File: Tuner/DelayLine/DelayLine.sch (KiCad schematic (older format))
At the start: 87 parts, among them J1 Conn_Coaxial, J10 Conn_Coaxial, J11 Conn_Coaxial, J12 Conn_Coaxial, J13 Conn_01x01, J14 Conn_01x01, J15 Conn_01x01, J16 Conn_01x01, J17 Conn_02x10_Odd_Even, J18 Conn_Coaxial, J19 Conn_Coaxial, J2 Conn_01x01, J20 Conn_Coaxial, J21 Conn_Coaxial, J22 Conn_Coaxial, J23 Conn_Coaxial, J24 Conn_01x01, J25 Conn_01x01, J26 Conn_01x01, J27 Conn_01x01, J28 Conn_01x01, J29 Conn_Coaxial, J3 Conn_Coaxial, J31 Conn_Coaxial, J32 Conn_01x01, J33 Conn_01x01, J34 Conn_01x01, J35 Conn_01x01, J5 Conn_Coaxial, J6 Conn_Coaxial, J7 Conn_Coaxial, J8 Conn_01x02, J9 Conn_01x02

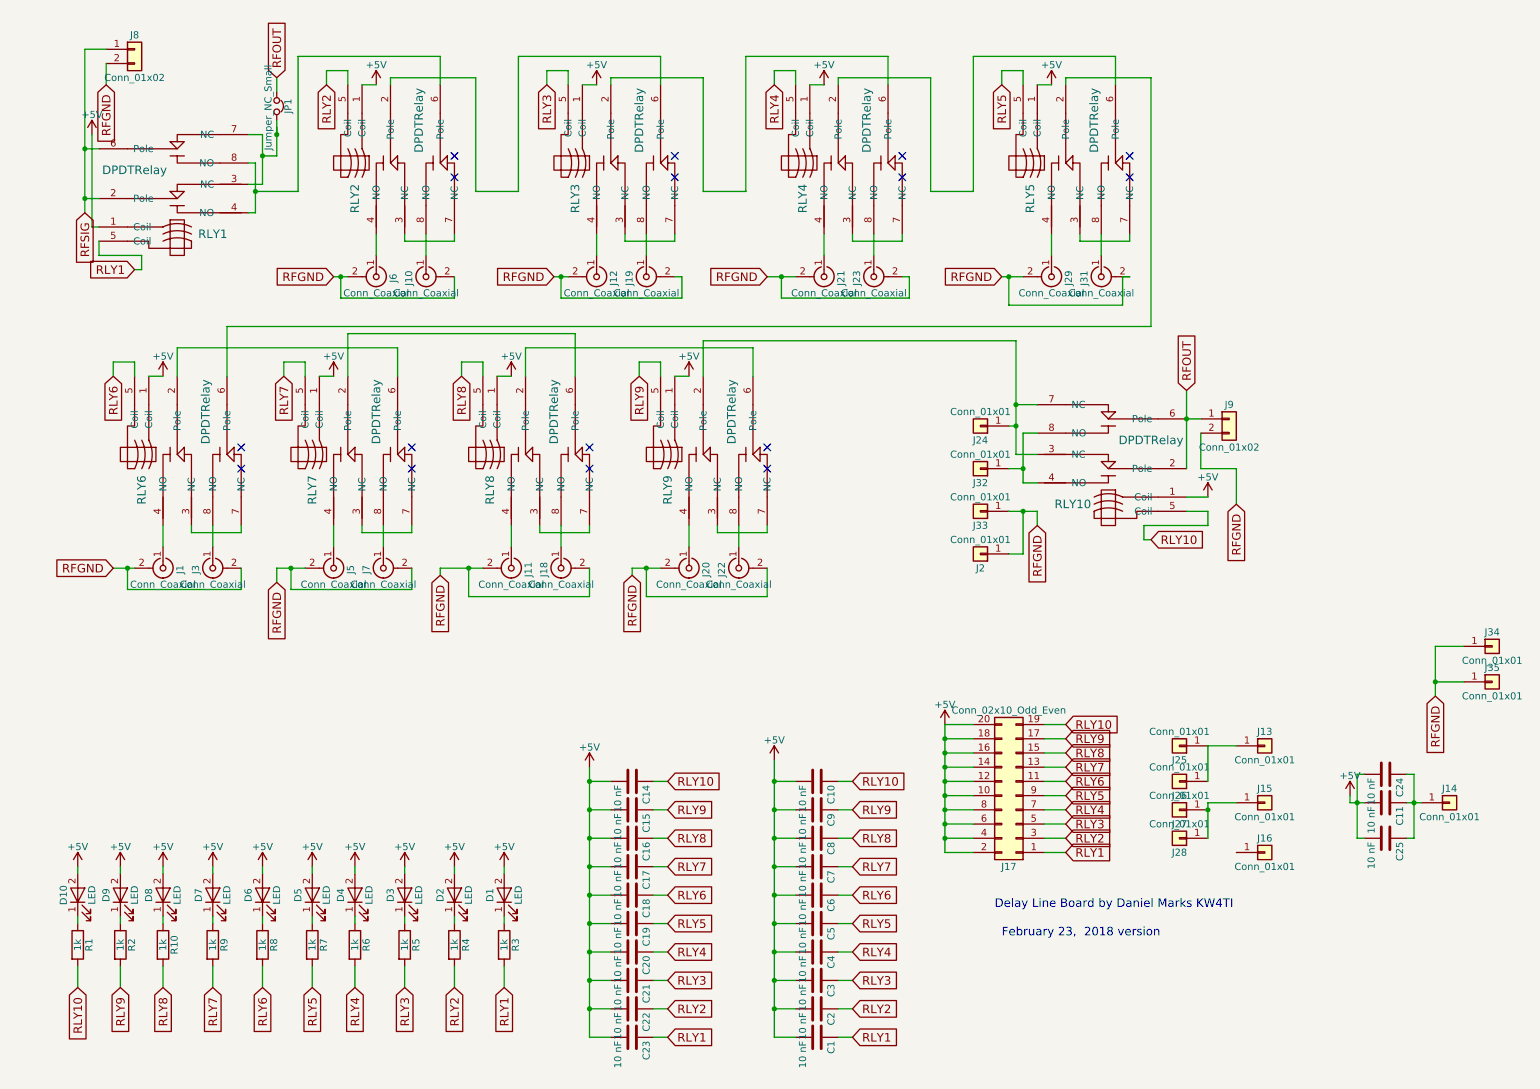
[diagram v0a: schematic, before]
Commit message: Changed bypass method on delay lines
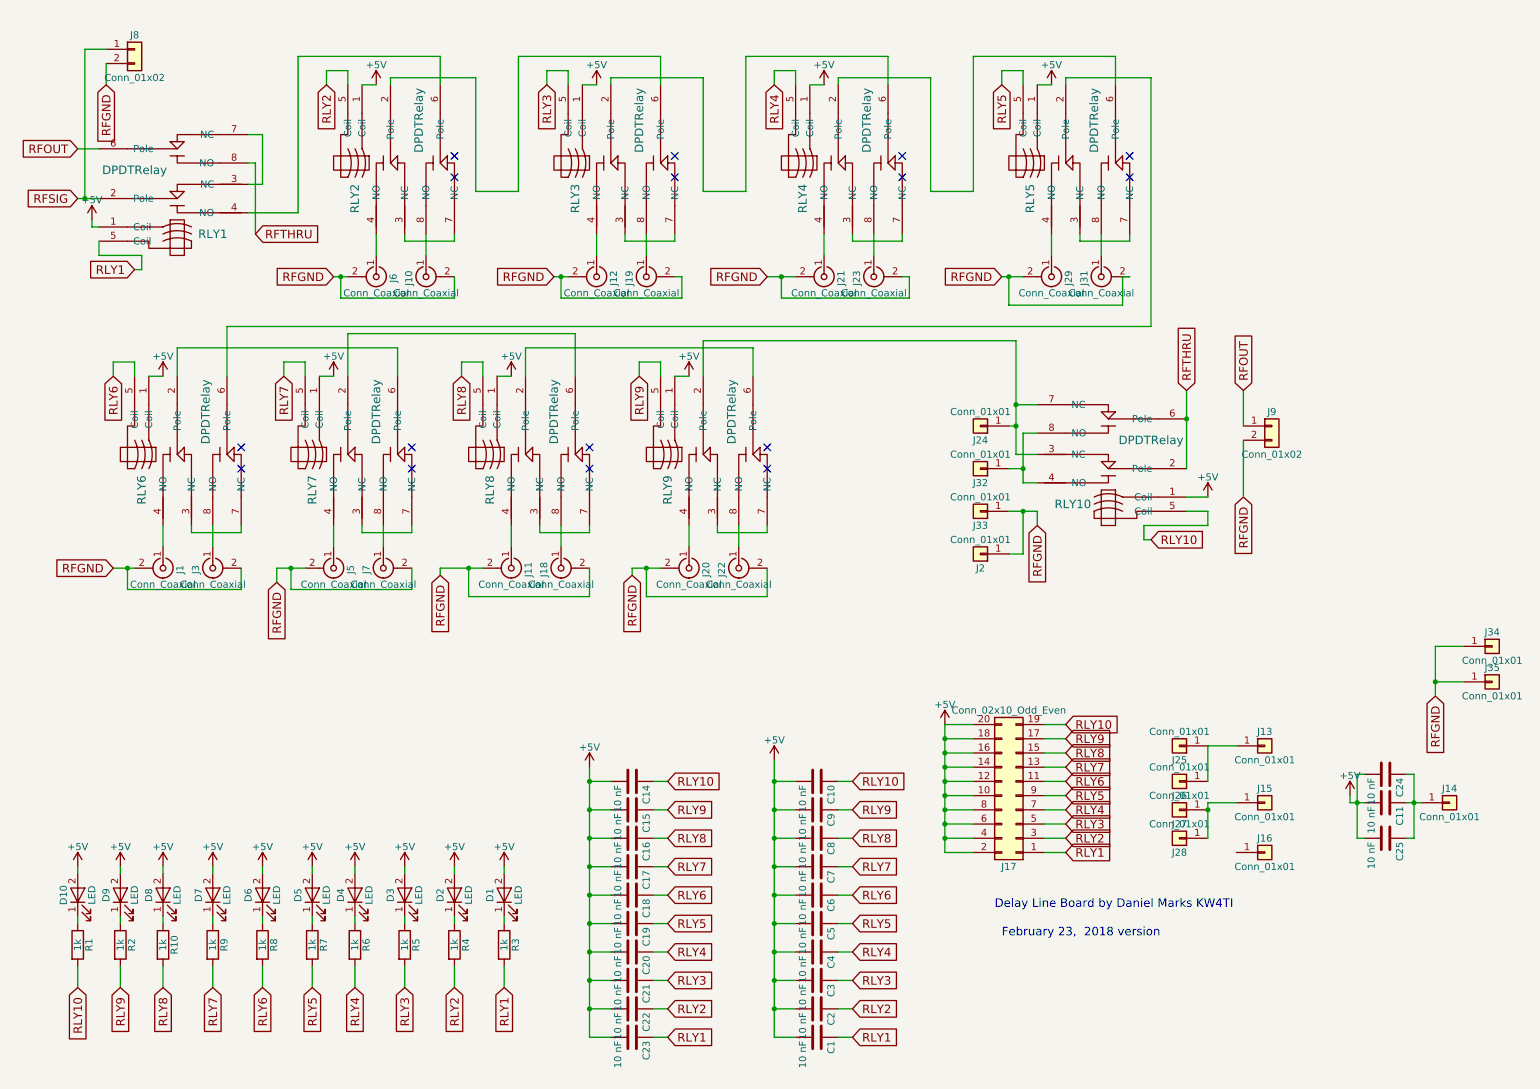
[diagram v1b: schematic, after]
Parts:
- removed JP1: Jumper_NC_Small, Pin_Headers:Pin_Header_Straight_1x02_Pitch2.54mm, symbol Jumper_NC_Small
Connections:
- net RFOUT: now also RLY1.6 (Pole); no longer RLY10.2 (Pole), RLY10.6 (Pole)
- net RFSIG: no longer RLY1.6 (Pole)
- net at RLY1.4 (NO), RLY2.6 (Pole): no longer RLY1.8 (NO)
- new net RFTHRU: RLY1.8 (NO), RLY10.2 (Pole), RLY10.6 (Pole)
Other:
- moved on the sheet: J9

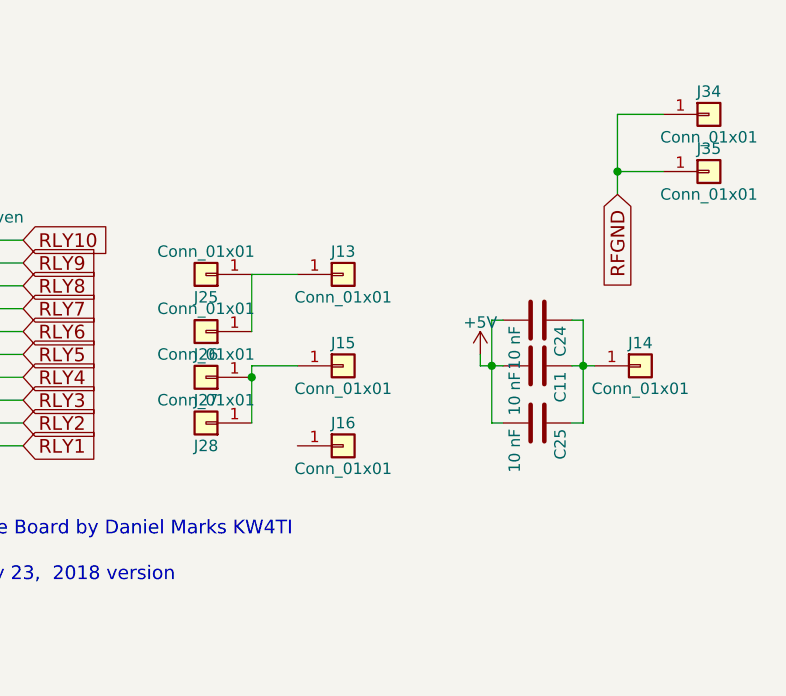
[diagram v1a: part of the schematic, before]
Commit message: Added extra capacitors between relay power and ground posts
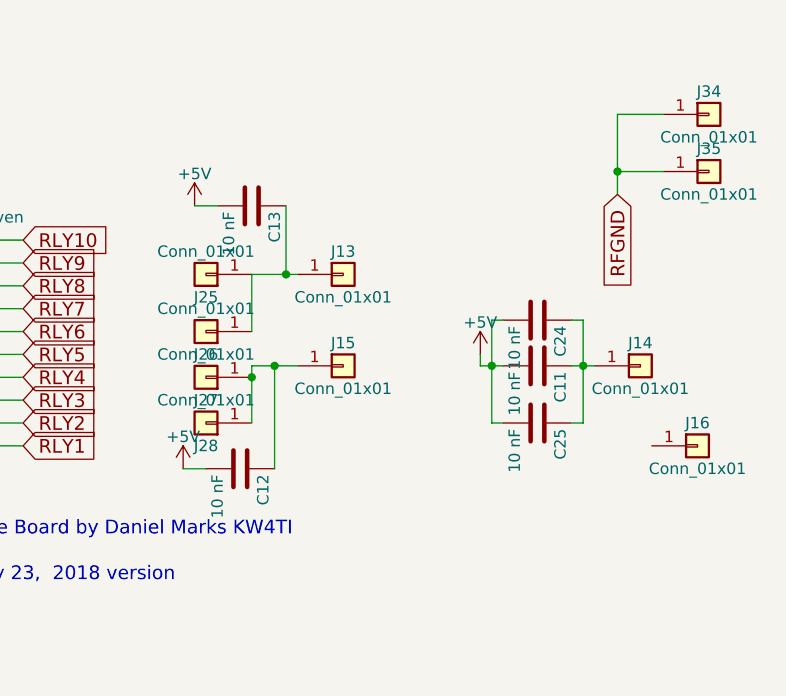
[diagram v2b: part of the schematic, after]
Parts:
- added C12, C13: 10 nF, Capacitors_THT:C_Disc_D5.0mm_W2.5mm_P2.50mm, symbol C
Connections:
- net +5V: now also C12.2, C13.2
- net at J13.1 (Pin_1), J25.1 (Pin_1), J26.1 (Pin_1): now also C13.1
- net at J15.1 (Pin_1), J27.1 (Pin_1), J28.1 (Pin_1): now also C12.1
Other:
- moved on the sheet: J16
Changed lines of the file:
@@
 $EndComp
 $Comp
-L +5V #PWR01
+L +5V #PWR2
 U 1 1 5B1A4DAD
 P 950 1850
-F 0 "#PWR01" H 950 1700 50  0001 C CNN
+F 0 "#PWR2" H 950 1700 50  0001 C CNN
 F 1 "+5V" H 950 1990 50  0000 C CNN
 F 2 "" H 950 1850 50  0001 C CNN
@@
 $EndComp
 $Comp
-L +5V #PWR02
+L +5V #PWR5
 U 1 1 5B25DE9C
 P 1450 6400
-F 0 "#PWR02" H 1450 6250 50  0001 C CNN
+F 0 "#PWR5" H 1450 6250 50  0001 C CNN
 F 1 "+5V" H 1450 6540 50  0000 C CNN
 F 2 "" H 1450 6400 50  0001 C CNN
@@
 $EndComp
 $Comp
-L +5V #PWR03
+L +5V #PWR6
 U 1 1 5B25F712
 P 1800 6400
-F 0 "#PWR03" H 1800 6250 50  0001 C CNN
+F 0 "#PWR6" H 1800 6250 50  0001 C CNN
 F 1 "+5V" H 1800 6540 50  0000 C CNN
 F 2 "" H 1800 6400 50  0001 C CNN
@@
 $EndComp
 $Comp
-L +5V #PWR04
+L +5V #PWR7
 U 1 1 5B25F91B
 P 2150 6400
-F 0 "#PWR04" H 2150 6250 50  0001 C CNN
+F 0 "#PWR7" H 2150 6250 50  0001 C CNN
 F 1 "+5V" H 2150 6540 50  0000 C CNN
 F 2 "" H 2150 6400 50  0001 C CNN
@@
 $EndComp
 $Comp
-L +5V #PWR05
+L +5V #PWR8
 U 1 1 5B25F931
 P 2500 6400
-F 0 "#PWR05" H 2500 6250 50  0001 C CNN
+F 0 "#PWR8" H 2500 6250 50  0001 C CNN
 F 1 "+5V" H 2500 6540 50  0000 C CNN
 F 2 "" H 2500 6400 50  0001 C CNN
@@
 $EndComp
 $Comp
-L +5V #PWR06
+L +5V #PWR10
 U 1 1 5B25FB4D
 P 2800 6400
-F 0 "#PWR06" H 2800 6250 50  0001 C CNN
+F 0 "#PWR10" H 2800 6250 50  0001 C CNN
 F 1 "+5V" H 2800 6540 50  0000 C CNN
 F 2 "" H 2800 6400 50  0001 C CNN
@@
 $EndComp
 $Comp
-L +5V #PWR07
+L +5V #PWR12
 U 1 1 5B25FB63
 P 3150 6400
-F 0 "#PWR07" H 3150 6250 50  0001 C CNN
+F 0 "#PWR12" H 3150 6250 50  0001 C CNN
 F 1 "+5V" H 3150 6540 50  0000 C CNN
 F 2 "" H 3150 6400 50  0001 C CNN
@@
 $EndComp
 $Comp
-L +5V #PWR08
+L +5V #PWR13
 U 1 1 5B25FB79
 P 3500 6400
-F 0 "#PWR08" H 3500 6250 50  0001 C CNN
+F 0 "#PWR13" H 3500 6250 50  0001 C CNN
 F 1 "+5V" H 3500 6540 50  0000 C CNN
 F 2 "" H 3500 6400 50  0001 C CNN
@@
 $EndComp
 $Comp
-L +5V #PWR09
+L +5V #PWR14
 U 1 1 5B25FB8F
 P 3850 6400
-F 0 "#PWR09" H 3850 6250 50  0001 C CNN
+F 0 "#PWR14" H 3850 6250 50  0001 C CNN
 F 1 "+5V" H 3850 6540 50  0000 C CNN
 F 2 "" H 3850 6400 50  0001 C CNN
@@
 RLY10
 $Comp
-L +5V #PWR010
+L +5V #PWR21
 U 1 1 5B89A678
 P 6950 5400
-F 0 "#PWR010" H 6950 5250 50  0001 C CNN
+F 0 "#PWR21" H 6950 5250 50  0001 C CNN
 F 1 "+5V" H 6950 5540 50  0000 C CNN
 F 2 "" H 6950 5400 50  0001 C CNN
@@
 $EndComp
 $Comp
-L +5V #PWR011
+L +5V #PWR3
 U 1 1 5B89BB19
 P 1150 6400
-F 0 "#PWR011" H 1150 6250 50  0001 C CNN
+F 0 "#PWR3" H 1150 6250 50  0001 C CNN
 F 1 "+5V" H 1150 6540 50  0000 C CNN
 F 2 "" H 1150 6400 50  0001 C CNN
@@
 $EndComp
 $Comp
-L +5V #PWR012
+L +5V #PWR1
 U 1 1 5B89BBCB
 P 850 6400
-F 0 "#PWR012" H 850 6250 50  0001 C CNN
+F 0 "#PWR1" H 850 6250 50  0001 C CNN
 F 1 "+5V" H 850 6540 50  0000 C CNN
 F 2 "" H 850 6400 50  0001 C CNN
@@
 RLY9
 $Comp
-L +5V #PWR013
+L +5V #PWR19
 U 1 1 5B89FB34
 P 5750 5650
-F 0 "#PWR013" H 5750 5500 50  0001 C CNN
+F 0 "#PWR19" H 5750 5500 50  0001 C CNN
 F 1 "+5V" H 5750 5790 50  0000 C CNN
 F 2 "" H 5750 5650 50  0001 C CNN
@@
 $EndComp
 $Comp
-L +5V #PWR014
+L +5V #PWR26
 U 1 1 5B97C780
 P 9800 5900
-F 0 "#PWR014" H 9800 5750 50  0001 C CNN
+F 0 "#PWR26" H 9800 5750 50  0001 C CNN
 F 1 "+5V" H 9800 6040 50  0000 C CNN
 F 2 "" H 9800 5900 50  0001 C CNN
@@
 RLY9
 $Comp
-L +5V #PWR015
+L +5V #PWR16
 U 1 1 5BA3849B
 P 4450 5700
-F 0 "#PWR015" H 4450 5550 50  0001 C CNN
+F 0 "#PWR16" H 4450 5550 50  0001 C CNN
 F 1 "+5V" H 4450 5840 50  0000 C CNN
 F 2 "" H 4450 5700 50  0001 C CNN
@@
 L Conn_01x01 J16
 U 1 1 5C727F83
-P 9200 6300
-F 0 "J16" H 9200 6400 50  0000 C CNN
-F 1 "Conn_01x01" H 9200 6200 50  0000 C CNN
-F 2 "Connectors:1pin" H 9200 6300 50  0001 C CNN
-F 3 "" H 9200 6300 50  0001 C CNN
-	1    9200 6300
+P 10750 6300
+F 0 "J16" H 10750 6400 50  0000 C CNN
+F 1 "Conn_01x01" H 10750 6200 50  0000 C CNN
+F 2 "Connectors:1pin" H 10750 6300 50  0001 C CNN
+F 3 "" H 10750 6300 50  0001 C CNN
+	1    10750 6300
 	1    0    0    -1
 $EndComp
@@
 RLY2
 $Comp
-L +5V #PWR016
+L +5V #PWR11
 U 1 1 5C733753
 P 2950 900
-F 0 "#PWR016" H 2950 750 50  0001 C CNN
+F 0 "#PWR11" H 2950 750 50  0001 C CNN
 F 1 "+5V" H 2950 1040 50  0000 C CNN
 F 2 "" H 2950 900 50  0001 C CNN
@@
 RLY10
 $Comp
-L +5V #PWR017
+L +5V #PWR25
 U 1 1 5C7350A4
 P 8800 3800
-F 0 "#PWR017" H 8800 3650 50  0001 C CNN
+F 0 "#PWR25" H 8800 3650 50  0001 C CNN
 F 1 "+5V" H 8800 3940 50  0000 C CNN
 F 2 "" H 8800 3800 50  0001 C CNN
@@
 RLY3
 $Comp
-L +5V #PWR018
+L +5V #PWR17
 U 1 1 5C759EA2
 P 4500 900
-F 0 "#PWR018" H 4500 750 50  0001 C CNN
+F 0 "#PWR17" H 4500 750 50  0001 C CNN
 F 1 "+5V" H 4500 1040 50  0000 C CNN
 F 2 "" H 4500 900 50  0001 C CNN
@@
 RLY4
 $Comp
-L +5V #PWR019
+L +5V #PWR20
 U 1 1 5C75A6EF
 P 6100 900
-F 0 "#PWR019" H 6100 750 50  0001 C CNN
+F 0 "#PWR20" H 6100 750 50  0001 C CNN
 F 1 "+5V" H 6100 1040 50  0000 C CNN
 F 2 "" H 6100 900 50  0001 C CNN
@@
 RLY5
 $Comp
-L +5V #PWR020
+L +5V #PWR22
 U 1 1 5C75AF8D
 P 7700 900
-F 0 "#PWR020" H 7700 750 50  0001 C CNN
+F 0 "#PWR22" H 7700 750 50  0001 C CNN
 F 1 "+5V" H 7700 1040 50  0000 C CNN
 F 2 "" H 7700 900 50  0001 C CNN
@@
 RLY6
 $Comp
-L +5V #PWR021
+L +5V #PWR4
 U 1 1 5C75CACE
 P 1450 2950
-F 0 "#PWR021" H 1450 2800 50  0001 C CNN
+F 0 "#PWR4" H 1450 2800 50  0001 C CNN
 F 1 "+5V" H 1450 3090 50  0000 C CNN
 F 2 "" H 1450 2950 50  0001 C CNN
@@
 RLY7
 $Comp
-L +5V #PWR022
+L +5V #PWR9
 U 1 1 5C75D7A5
 P 2650 2950
-F 0 "#PWR022" H 2650 2800 50  0001 C CNN
+F 0 "#PWR9" H 2650 2800 50  0001 C CNN
 F 1 "+5V" H 2650 3090 50  0000 C CNN
 F 2 "" H 2650 2950 50  0001 C CNN
@@
 RLY8
 $Comp
-L +5V #PWR023
+L +5V #PWR15
 U 1 1 5C75E937
 P 3900 2950
-F 0 "#PWR023" H 3900 2800 50  0001 C CNN
+F 0 "#PWR15" H 3900 2800 50  0001 C CNN
 F 1 "+5V" H 3900 3090 50  0000 C CNN
 F 2 "" H 3900 2950 50  0001 C CNN
@@
 RLY9
 $Comp
-L +5V #PWR024
+L +5V #PWR18
 U 1 1 5C75F12E
 P 5150 2950
-F 0 "#PWR024" H 5150 2800 50  0001 C CNN
+F 0 "#PWR18" H 5150 2800 50  0001 C CNN
 F 1 "+5V" H 5150 3090 50  0000 C CNN
 F 2 "" H 5150 2950 50  0001 C CNN
@@
 	900  650  1050 650
 Connection ~ 900  1700
+$Comp
+L +5V #PWR24
+U 1 1 5DDBBCDB
+P 8550 5250
+F 0 "#PWR24" H 8550 5100 50  0001 C CNN
+F 1 "+5V" H 8550 5390 50  0000 C CNN
+F 2 "" H 8550 5250 50  0001 C CNN
+F 3 "" H 8550 5250 50  0001 C CNN
+	1    8550 5250
+	1    0    0    -1
+$EndComp
+$Comp
+L C C13
+U 1 1 5DDBBF5C
+P 8800 5250
+F 0 "C13" H 8825 5350 50  0000 L CNN
+F 1 "10 nF" H 8825 5150 50  0000 L CNN
+F 2 "Capacitors_THT:C_Disc_D5.0mm_W2.5mm_P2.50mm" H 8838 5100 50  0001 C CNN
+F 3 "" H 8800 5250 50  0001 C CNN
+	1    8800 5250
+	0    1    1    0
+$EndComp
+Wire Wire Line
+	8650 5250 8550 5250
+Wire Wire Line
+	8950 5250 8950 5550
+Connection ~ 8950 5550
+$Comp
+L C C12
+U 1 1 5DDBC710
+P 8750 6400
+F 0 "C12" H 8775 6500 50  0000 L CNN
+F 1 "10 nF" H 8775 6300 50  0000 L CNN
+F 2 "Capacitors_THT:C_Disc_D5.0mm_W2.5mm_P2.50mm" H 8788 6250 50  0001 C CNN
+F 3 "" H 8750 6400 50  0001 C CNN
+	1    8750 6400
+	0    1    1    0
+$EndComp
+$Comp
+L +5V #PWR23
+U 1 1 5DDBC836
+P 8500 6400
+F 0 "#PWR23" H 8500 6250 50  0001 C CNN
+F 1 "+5V" H 8500 6540 50  0000 C CNN
+F 2 "" H 8500 6400 50  0001 C CNN
+F 3 "" H 8500 6400 50  0001 C CNN
+	1    8500 6400
+	1    0    0    -1
+$EndComp
+Wire Wire Line
+	8600 6400 8500 6400
+Wire Wire Line
+	8900 5950 8900 6400
+Connection ~ 8900 5950
 $EndSCHEMATC

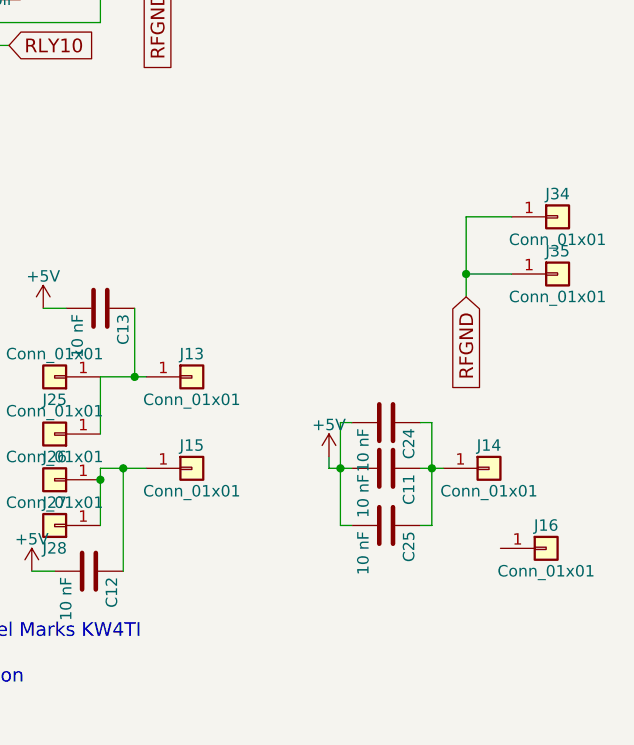
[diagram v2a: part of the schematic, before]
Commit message: Added extra capacitors to ground to large relay boards
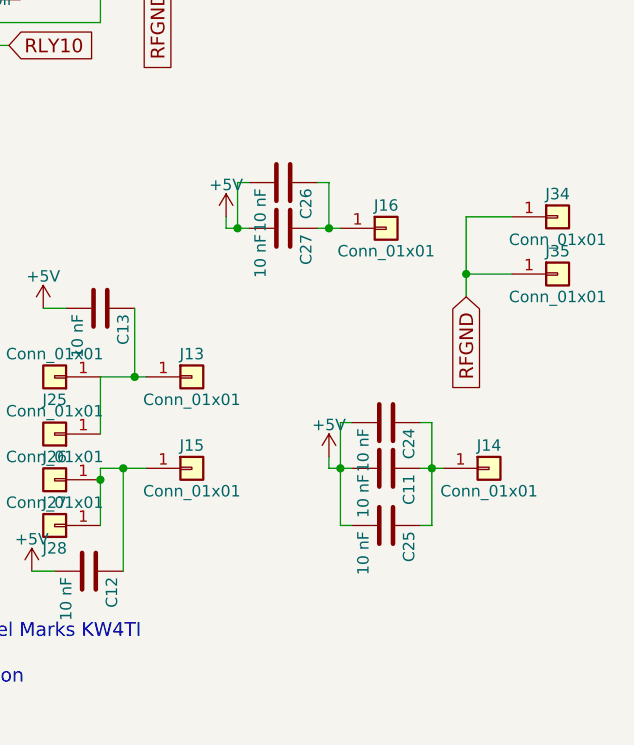
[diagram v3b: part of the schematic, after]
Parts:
- added C26, C27: 10 nF, Capacitors_THT:C_Disc_D5.0mm_W2.5mm_P5.00mm, symbol C
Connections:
- net +5V: now also C26.2, C27.2
- net at J16.1 (Pin_1): now also C26.1, C27.1
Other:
- moved on the sheet: J16
